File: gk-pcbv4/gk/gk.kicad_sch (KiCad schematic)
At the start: 11 parts

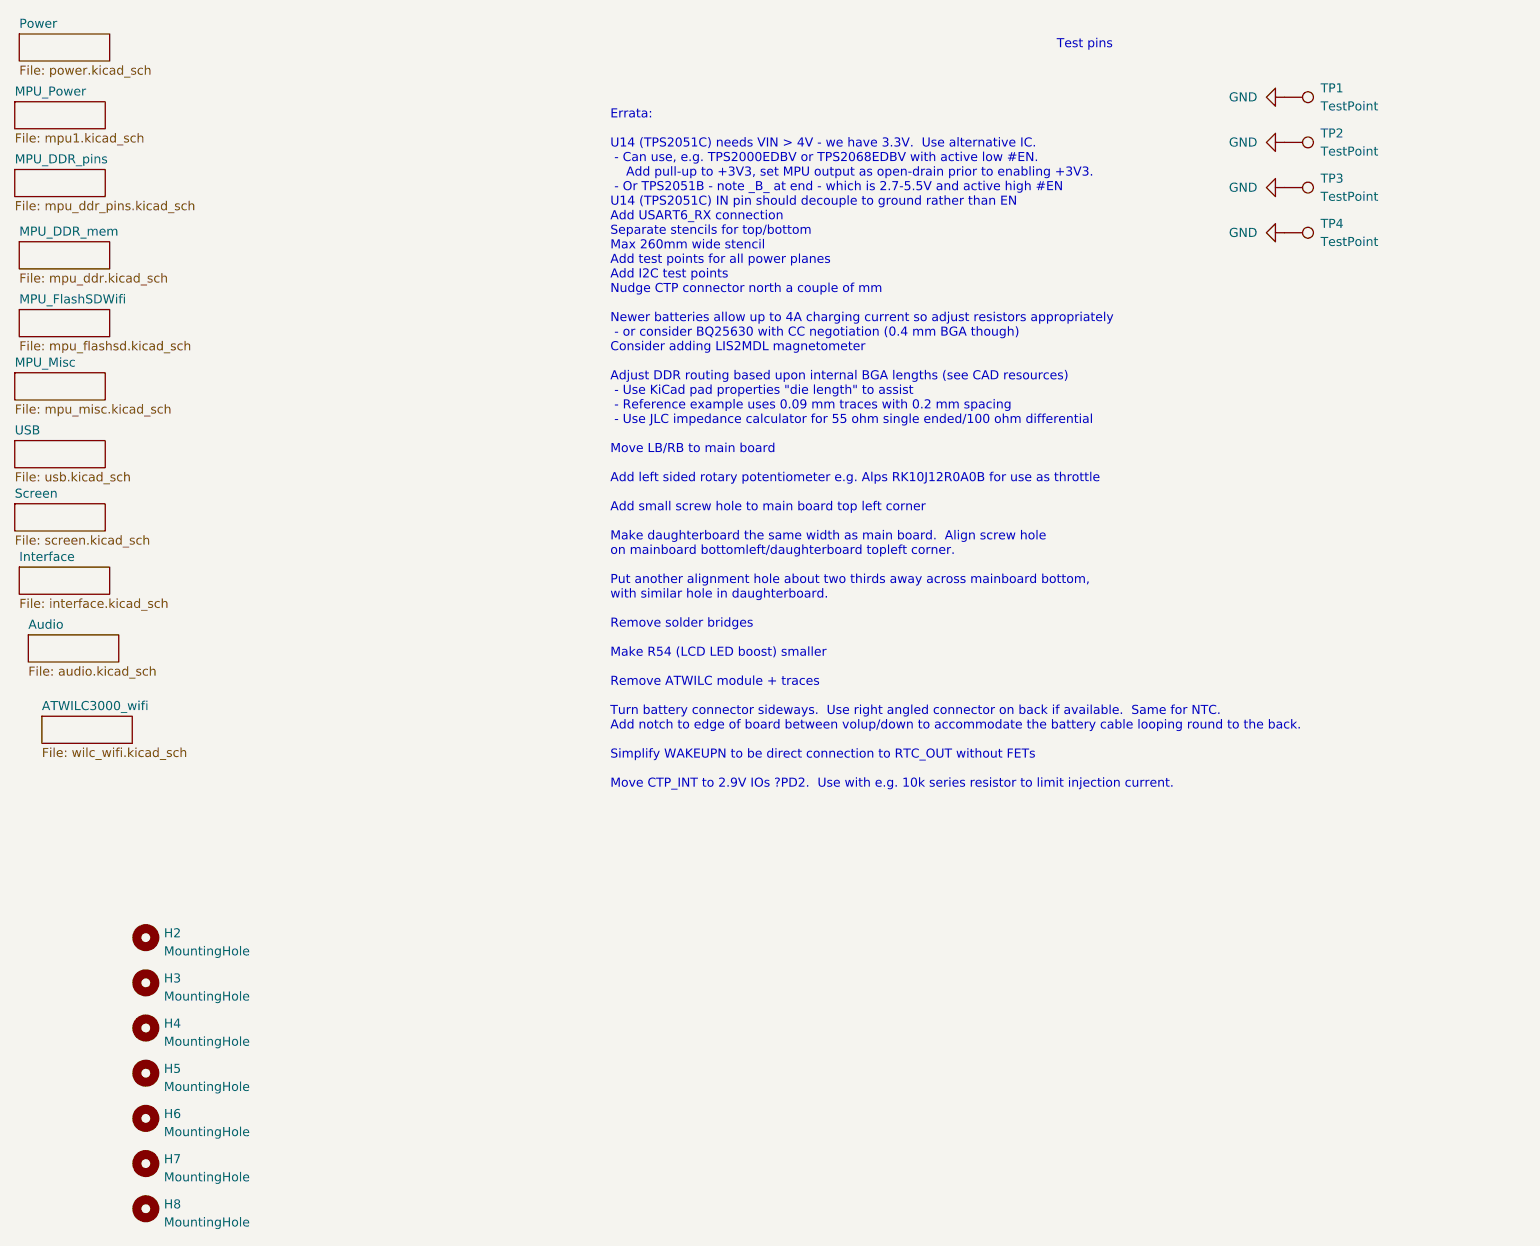
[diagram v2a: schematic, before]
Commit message: remove wilc chip
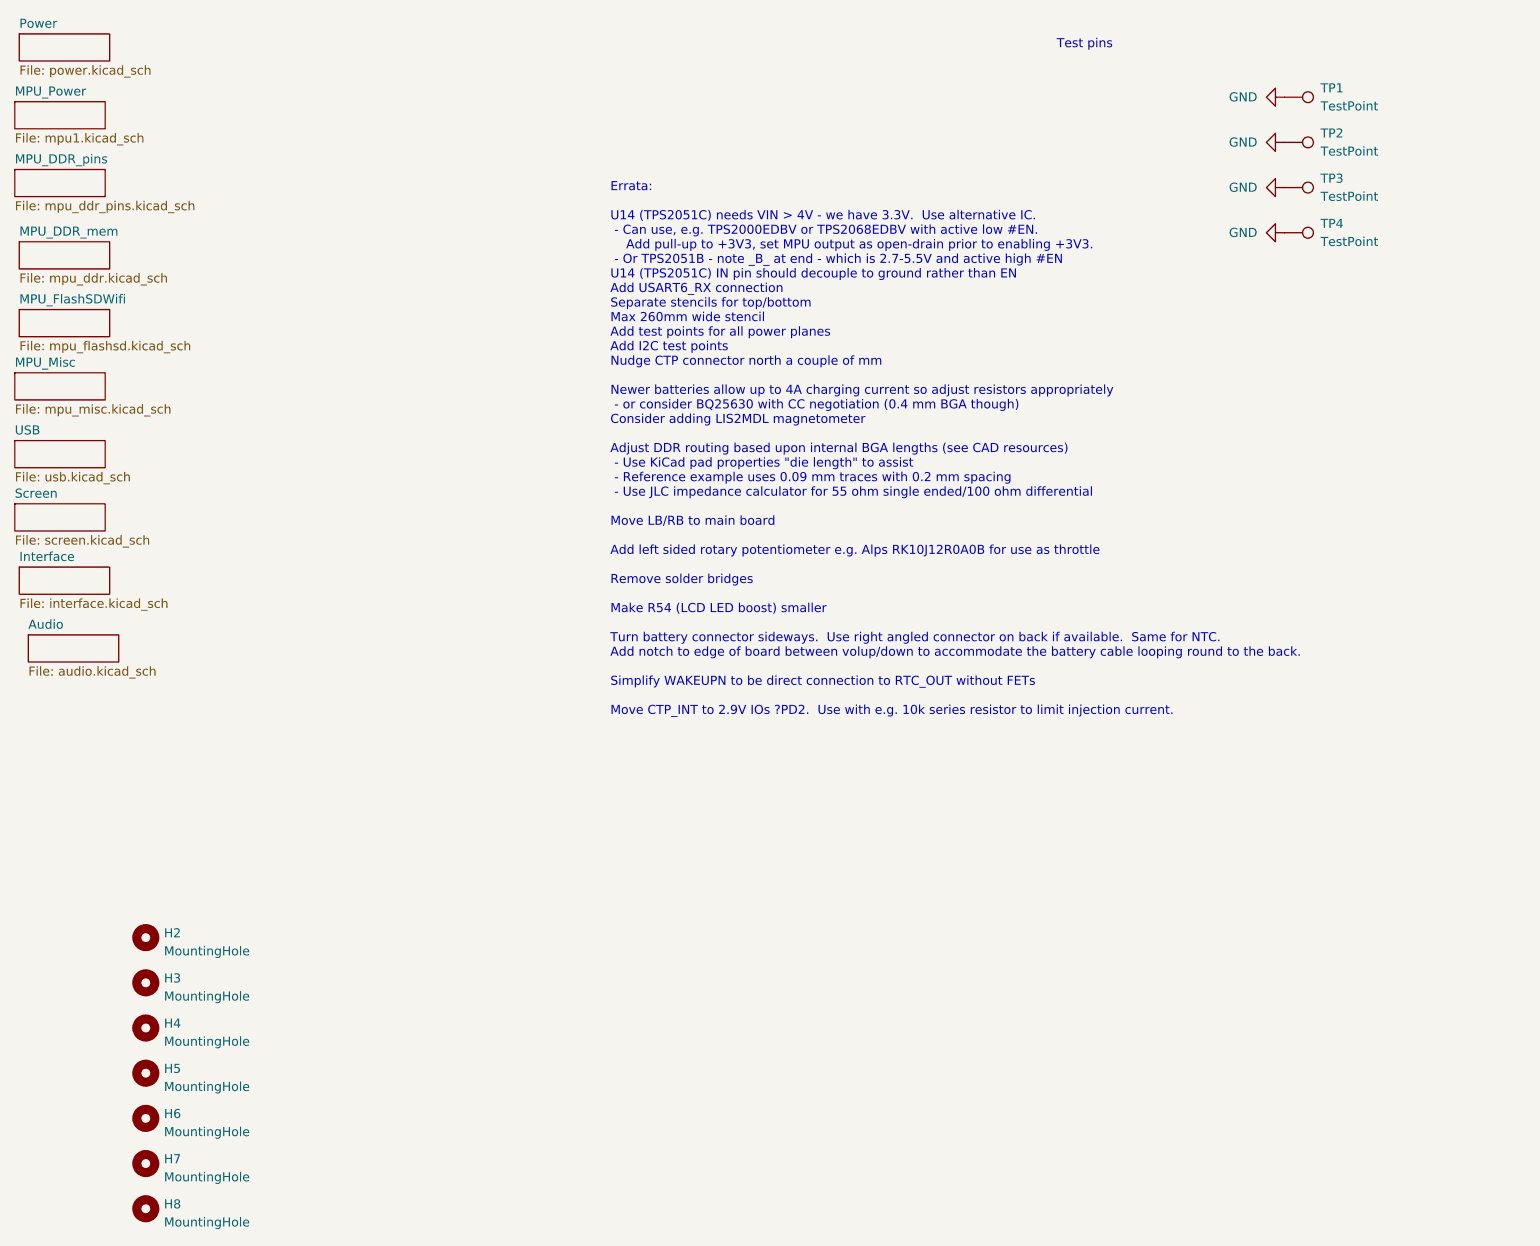
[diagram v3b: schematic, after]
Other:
- removed sheet ATWILC3000_wifi
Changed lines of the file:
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@@
 		)
 	)
-	(text "Errata:\n\nU14 (TPS2051C) needs VIN > 4V - we have 3.3V.  Use alternative IC.\n - Can use, e.g. TPS2000EDBV or TPS2068EDBV with active low #EN.\n    Add pull-up to +3V3, set MPU output as open-drain prior to enabling +3V3.\n - Or TPS2051B - note _B_ at end - which is 2.7-5.5V and active high #EN\nU14 (TPS2051C) IN pin should decouple to ground rather than EN\nAdd USART6_RX connection\nSeparate stencils for top/bottom\nMax 260mm wide stencil\nAdd test points for all power planes\nAdd I2C test points\nNudge CTP connector north a couple of mm\n\nNewer batteries allow up to 4A charging current so adjust resistors appropriately\n - or consider BQ25630 with CC negotiation (0.4 mm BGA though)\nConsider adding LIS2MDL magnetometer\n\nAdjust DDR routing based upon internal BGA lengths (see CAD resources)\n - Use KiCad pad properties \"die length\" to assist\n - Reference example uses 0.09 mm traces with 0.2 mm spacing\n - Use JLC impedance calculator for 55 ohm single ended/100 ohm differential\n\nMove LB/RB to main board\n\nAdd left sided rotary potentiometer e.g. Alps RK10J12R0A0B for use as throttle\n\nAdd small screw hole to main board top left corner\n\nMake daughterboard the same width as main board.  Align screw hole\non mainboard bottomleft/daughterboard topleft corner.\n\nPut another alignment hole about two thirds away across mainboard bottom,\nwith similar hole in daughterboard.\n\nRemove solder bridges\n\nMake R54 (LCD LED boost) smaller\n\nRemove ATWILC module + traces\n\nTurn battery connector sideways.  Use right angled connector on back if available.  Same for NTC.\nAdd notch to edge of board between volup/down to accommodate the battery cable looping round to the back.\n\nSimplify WAKEUPN to be direct connection to RTC_OUT without FETs\n\nMove CTP_INT to 2.9V IOs ?PD2.  Use with e.g. 10k series resistor to limit injection current."
+	(text "Errata:\n\nU14 (TPS2051C) needs VIN > 4V - we have 3.3V.  Use alternative IC.\n - Can use, e.g. TPS2000EDBV or TPS2068EDBV with active low #EN.\n    Add pull-up to +3V3, set MPU output as open-drain prior to enabling +3V3.\n - Or TPS2051B - note _B_ at end - which is 2.7-5.5V and active high #EN\nU14 (TPS2051C) IN pin should decouple to ground rather than EN\nAdd USART6_RX connection\nSeparate stencils for top/bottom\nMax 260mm wide stencil\nAdd test points for all power planes\nAdd I2C test points\nNudge CTP connector north a couple of mm\n\nNewer batteries allow up to 4A charging current so adjust resistors appropriately\n - or consider BQ25630 with CC negotiation (0.4 mm BGA though)\nConsider adding LIS2MDL magnetometer\n\nAdjust DDR routing based upon internal BGA lengths (see CAD resources)\n - Use KiCad pad properties \"die length\" to assist\n - Reference example uses 0.09 mm traces with 0.2 mm spacing\n - Use JLC impedance calculator for 55 ohm single ended/100 ohm differential\n\nMove LB/RB to main board\n\nAdd left sided rotary potentiometer e.g. Alps RK10J12R0A0B for use as throttle\n\nRemove solder bridges\n\nMake R54 (LCD LED boost) smaller\n\nTurn battery connector sideways.  Use right angled connector on back if available.  Same for NTC.\nAdd notch to edge of board between volup/down to accommodate the battery cable looping round to the back.\n\nSimplify WAKEUPN to be direct connection to RTC_OUT without FETs\n\nMove CTP_INT to 2.9V IOs ?PD2.  Use with e.g. 10k series resistor to limit injection current."
 		(exclude_from_sim no)
 		(at 104.648 80.01 0)
@@
 				)
 			)
-		)
-	)
-	(sheet
-		(at 24.765 117.475)
-		(size 12.7 3.81)
-		(exclude_from_sim no)
-		(in_bom yes)
-		(on_board yes)
-		(dnp no)
-		(fields_autoplaced yes)
-		(stroke
-			(width 0.1524)
-			(type solid)
-		)
-		(fill
-			(color 0 0 0 0.0000)
-		)
-		(property "Sheetname" "ATWILC3000_wifi"
-			(at 24.765 116.7634 0)
-			(effects
-				(font
-					(size 1.27 1.27)
-				)
-				(justify left bottom)
-			)
-		)
-		(property "Sheetfile" "wilc_wifi.kicad_sch"
-			(at 24.765 121.8696 0)
-			(effects
-				(font
-					(size 1.27 1.27)
-				)
-				(justify left top)
-			)
-		)
-		(instances
-			(project "gk"
-				(path "/a049c72e-5361-408c-ab21-661d491fee9d"
-					(page "12")
-				)
-			)

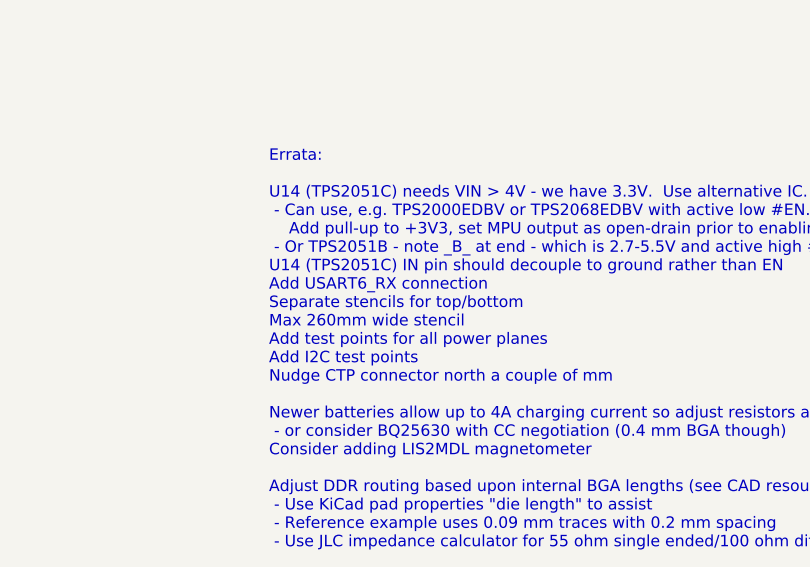
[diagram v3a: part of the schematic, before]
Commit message: add usart6 connection to schematic
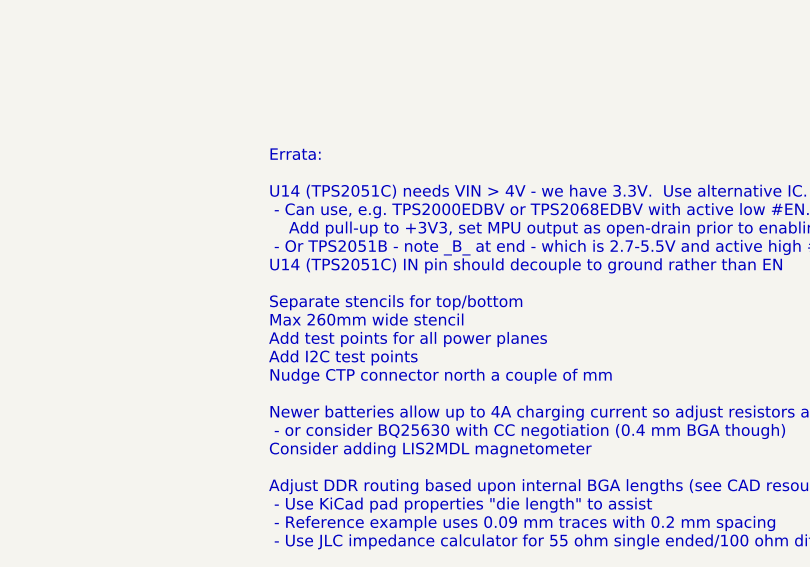
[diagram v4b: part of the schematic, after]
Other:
- note added: "Errata: U14 (TPS2051C) needs VIN > 4V - we have 3.3V. Use alternative IC. - Can use, e.g. TPS2000EDBV or TPS2068EDBV with active low #EN. Add pull-up to +3V3, set MPU output as open-drain prior to enabling +3V3. - Or TPS2051B - note _B_ at end - which is 2.7-5.5V and active high #EN U14 (TPS2051C) IN pin should decouple to ground rather than EN Separate stencils for top/bottom Max 260mm wide sten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"
- note removed: "Errata: U14 (TPS2051C) needs VIN > 4V - we have 3.3V. Use alternative IC. - Can use, e.g. TPS2000EDBV or TPS2068EDBV with active low #EN. Add pull-up to +3V3, set MPU output as open-drain prior to enabling +3V3. - Or TPS2051B - note _B_ at end - which is 2.7-5.5V and active high #EN U14 (TPS2051C) IN pin should decouple to ground rather than EN Add USART6_RX connection Separate stencils for top/b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"
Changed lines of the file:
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@@
 		)
 	)
-	(text "Errata:\n\nU14 (TPS2051C) needs VIN > 4V - we have 3.3V.  Use alternative IC.\n - Can use, e.g. TPS2000EDBV or TPS2068EDBV with active low #EN.\n    Add pull-up to +3V3, set MPU output as open-drain prior to enabling +3V3.\n - Or TPS2051B - note _B_ at end - which is 2.7-5.5V and active high #EN\nU14 (TPS2051C) IN pin should decouple to ground rather than EN\nAdd USART6_RX connection\nSeparate stencils for top/bottom\nMax 260mm wide stencil\nAdd test points for all power planes\nAdd I2C test points\nNudge CTP connector north a couple of mm\n\nNewer batteries allow up to 4A charging current so adjust resistors appropriately\n - or consider BQ25630 with CC negotiation (0.4 mm BGA though)\nConsider adding LIS2MDL magnetometer\n\nAdjust DDR routing based upon internal BGA lengths (see CAD resources)\n - Use KiCad pad properties \"die length\" to assist\n - Reference example uses 0.09 mm traces with 0.2 mm spacing\n - Use JLC impedance calculator for 55 ohm single ended/100 ohm differential\n\nMove LB/RB to main board\n\nAdd left sided rotary potentiometer e.g. Alps RK10J12R0A0B for use as throttle\n\nRemove solder bridges\n\nMake R54 (LCD LED boost) smaller\n\nTurn battery connector sideways.  Use right angled connector on back if available.  Same for NTC.\nAdd notch to edge of board between volup/down to accommodate the battery cable looping round to the back.\n\nSimplify WAKEUPN to be direct connection to RTC_OUT without FETs\n\nMove CTP_INT to 2.9V IOs ?PD2.  Use with e.g. 10k series resistor to limit injection current."
+	(text "Errata:\n\nU14 (TPS2051C) needs VIN > 4V - we have 3.3V.  Use alternative IC.\n - Can use, e.g. TPS2000EDBV or TPS2068EDBV with active low #EN.\n    Add pull-up to +3V3, set MPU output as open-drain prior to enabling +3V3.\n - Or TPS2051B - note _B_ at end - which is 2.7-5.5V and active high #EN\nU14 (TPS2051C) IN pin should decouple to ground rather than EN\n\nSeparate stencils for top/bottom\nMax 260mm wide stencil\nAdd test points for all power planes\nAdd I2C test points\nNudge CTP connector north a couple of mm\n\nNewer batteries allow up to 4A charging current so adjust resistors appropriately\n - or consider BQ25630 with CC negotiation (0.4 mm BGA though)\nConsider adding LIS2MDL magnetometer\n\nAdjust DDR routing based upon internal BGA lengths (see CAD resources)\n - Use KiCad pad properties \"die length\" to assist\n - Reference example uses 0.09 mm traces with 0.2 mm spacing\n - Use JLC impedance calculator for 55 ohm single ended/100 ohm differential\n\nMove LB/RB to main board\n\nAdd left sided rotary potentiometer e.g. Alps RK10J12R0A0B for use as throttle\n\nRemove solder bridges\n\nMake R54 (LCD LED boost) smaller\n\nTurn battery connector sideways.  Use right angled connector on back if available.  Same for NTC.\nAdd notch to edge of board between volup/down to accommodate the battery cable looping round to the back.\n\nSimplify WAKEUPN to be direct connection to RTC_OUT without FETs\n\nMove CTP_INT to 2.9V IOs ?PD2.  Use with e.g. 10k series resistor to limit injection current."
 		(exclude_from_sim no)
 		(at 104.648 80.01 0)
